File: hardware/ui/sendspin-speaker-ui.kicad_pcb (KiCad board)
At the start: 2 copper layers, 0 parts

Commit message: hardware: footprints and nets in all three boards, JLC design rules
- Update PCB from Schematic on main, front panel and USB-C board.
- Design rules for JLCPCB 2-layer (0.15 mm track/clearance, 0.3 mm
  drill, 0.6 mm vias, 0.3 mm to the edge); net classes Power (1.0 mm),
  Speaker (0.6 mm), Supply3V3 (0.4 mm).
- TP4056 on the SOIC-8-EP footprint without 0.2 mm thermal vias;
  MSK12C02 footprint marked SMD, its shell pads to GND.
- Generator keeps symbol UUIDs stable so regenerated sheets stay linked.

Co-Authored-By: Claude Opus 5.5 <noreply@anthropic.com>
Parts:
- added C601: 100n, Capacitor_SMD:C_0805_2012Metric, F.Cu at (154.8, 142.9)
- added C602: 1u, Capacitor_SMD:C_0805_2012Metric, F.Cu at (154.8, 145.9)
- added D601: status, LED_SMD:LED_0805_2012Metric, F.Cu at (159.4, 120.5)
- added J601: J_UI, Connector_JST:JST_XH_B12B-XH-A_1x12_P2.50mm_Vertical, F.Cu at (145.5, 102.4)
- added J602: SPI display, Connector_PinHeader_2.54mm:PinHeader_1x08_P2.54mm_Vertical, F.Cu at (154.8, 121.3)
- added J603: I2C OLED, Connector_PinHeader_2.54mm:PinHeader_1x04_P2.54mm_Vertical, F.Cu at (154.8, 109.1)
- added R601: 10k, Resistor_SMD:R_0805_2012Metric, F.Cu at (159.3, 123.5)
- added R602: 1k, Resistor_SMD:R_0805_2012Metric, F.Cu at (159.3, 126.5)
- added SW601: Play/Pause, Button_Switch_THT:SW_PUSH_6mm, F.Cu at (144.0, 108.8)
- added SW603: Prev, Button_Switch_THT:SW_PUSH_6mm, F.Cu at (144.0, 117.4)
- added SW604: Next, Button_Switch_THT:SW_PUSH_6mm, F.Cu at (144.0, 125.9)
- added SW605: Vol -, Button_Switch_THT:SW_PUSH_6mm, F.Cu at (144.0, 134.5)
- added SW606: Vol +, Button_Switch_THT:SW_PUSH_6mm, F.Cu at (144.0, 143.0)

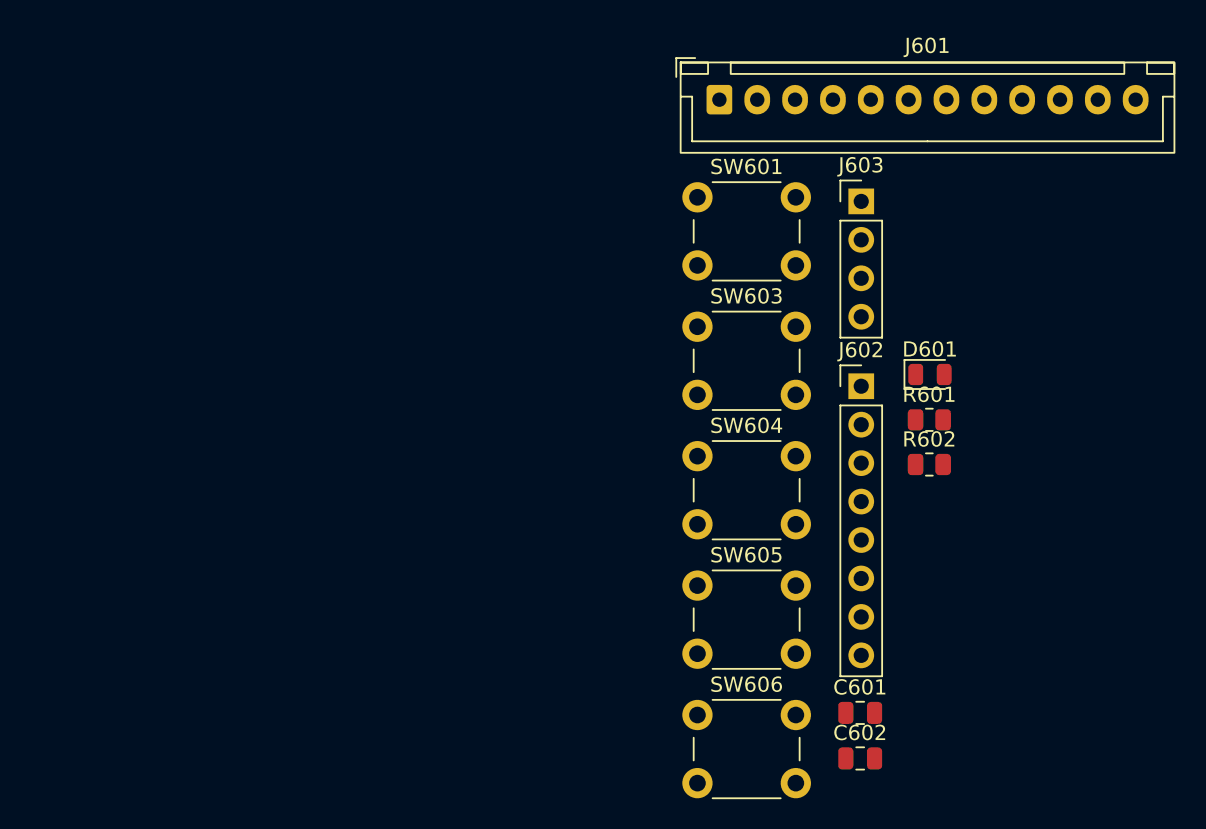
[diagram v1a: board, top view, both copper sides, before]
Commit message: hardware: first placement of all three boards
Outlines, mounting holes, edge connectors, parts by function and GND
pours, written with KiCad's Python (scripts/pcbplace.py, place_*.py).
DRC: no copper or courtyard errors; unrouted connections and silkscreen
text remain. Renders in hardware/docs/.

Co-Authored-By: Claude Opus 5.5 <noreply@anthropic.com>
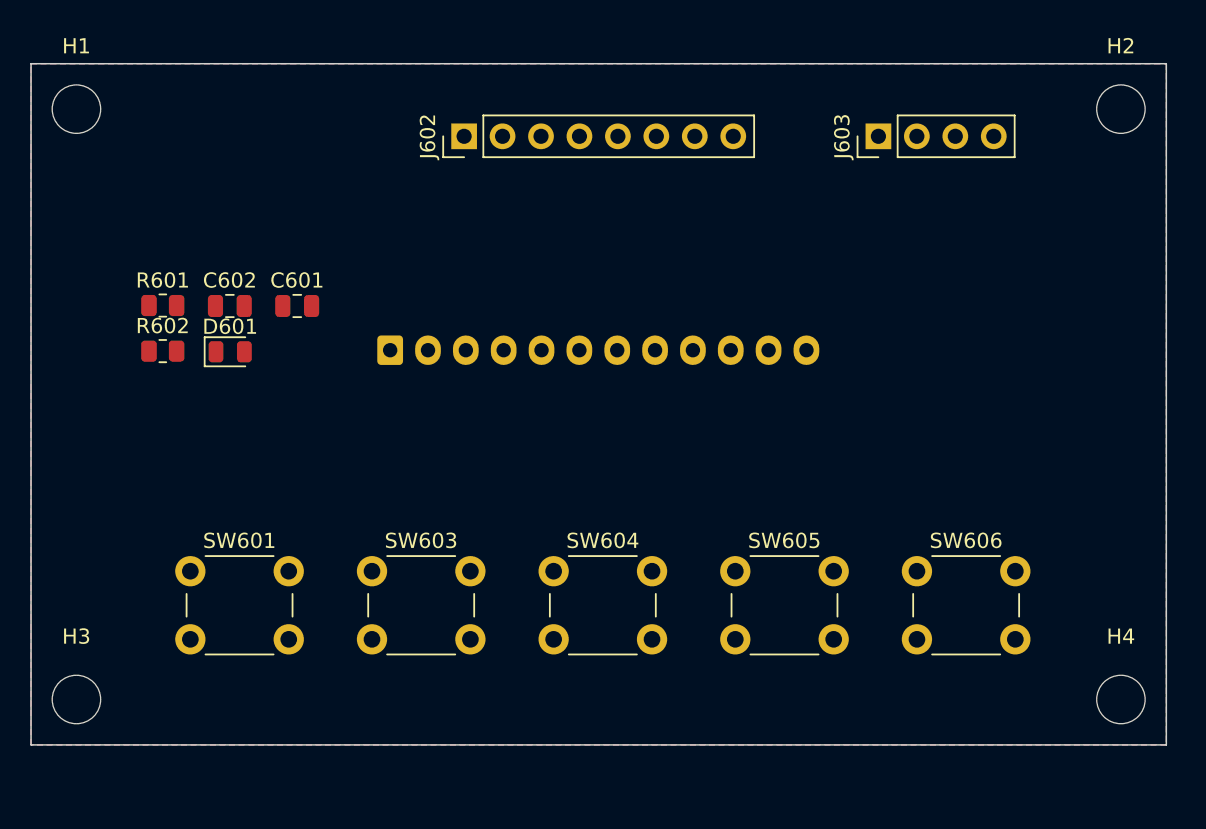
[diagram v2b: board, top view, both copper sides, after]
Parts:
- added H1: MountingHole_3.2mm_M3, MountingHole:MountingHole_3.2mm_M3, F.Cu at (103.0, 103.0)
- added H2: MountingHole_3.2mm_M3, MountingHole:MountingHole_3.2mm_M3, F.Cu at (172.0, 103.0)
- added H3: MountingHole_3.2mm_M3, MountingHole:MountingHole_3.2mm_M3, F.Cu at (103.0, 142.0)
- added H4: MountingHole_3.2mm_M3, MountingHole:MountingHole_3.2mm_M3, F.Cu at (172.0, 142.0)
- J601: moved to B.Cu
- moved C602 51.3 mm to (113.1, 116.0)
- moved R601 51.2 mm to (108.7, 116.0)
- moved R602 51.2 mm to (108.7, 119.0)
- moved D601 46.3 mm to (113.2, 119.0)
- moved C601 45.9 mm to (117.6, 116.0)
- moved SW601 41.6 mm to (110.5, 133.5)
- moved J602 31.0 mm to (128.6, 104.8), turned to 90 degrees
- moved J601 27.3 mm to (123.7, 118.9)
- moved SW603 26.9 mm to (122.5, 133.5)
- moved SW606 17.3 mm to (158.5, 133.5)
- moved SW604 12.2 mm to (134.5, 133.5)
- moved J603 4.45 mm to (156.0, 104.8), turned to 90 degrees
- moved SW605 2.67 mm to (146.5, 133.5)
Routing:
- added copper zone on B.Cu, net GND
- added copper zone on F.Cu, net GND
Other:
- board outline added: 75 x 45 mm

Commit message: hardware: bare panel/USB-C boards updated, XH battery, holes in, round corners
- Boards updated from the schematics: J_USB XH 6 with CC1/CC2, panel
  without parts (J604 LED header), USB-C board without parts.
- J_BAT JST XH 2.
- M3 holes 4.5 mm in from the edges (heads stay on the board), M2 3 mm;
  rounded corners. DRC: no copper, courtyard or outline errors.

Co-Authored-By: Claude Opus 5.5 <noreply@anthropic.com>
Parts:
- removed C601: 100n, Capacitor_SMD:C_0805_2012Metric
- removed C602: 1u, Capacitor_SMD:C_0805_2012Metric
- removed D601: status, LED_SMD:LED_0805_2012Metric
- removed R601: 10k, Resistor_SMD:R_0805_2012Metric
- removed R602: 1k, Resistor_SMD:R_0805_2012Metric
- added J604: LED, Connector_PinHeader_2.54mm:PinHeader_1x02_P2.54mm_Vertical, F.Cu at (111.8, 117.8)
- moved H1 2.12 mm to (104.5, 104.5)
- moved H2 2.12 mm to (170.5, 104.5)
- moved H3 2.12 mm to (104.5, 140.5)
- moved H4 2.12 mm to (170.5, 140.5)
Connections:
- J602 pad 7: /DISP_RST -> +3V3
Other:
- outline, holes or cut-outs redrawn
